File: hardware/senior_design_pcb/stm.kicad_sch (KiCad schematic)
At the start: 44 parts, among them J1 SBH11-PBPC-D05-ST-BK, J2 USB_C_Receptacle_USB2.0_16P, SW1 SW_Push, U1 LD1117S33TR_SOT223, U2 STM32F091RCTx, U3 FT232RL, X1 32.768kHz(12.5pF), X3 8MHz(20pF)

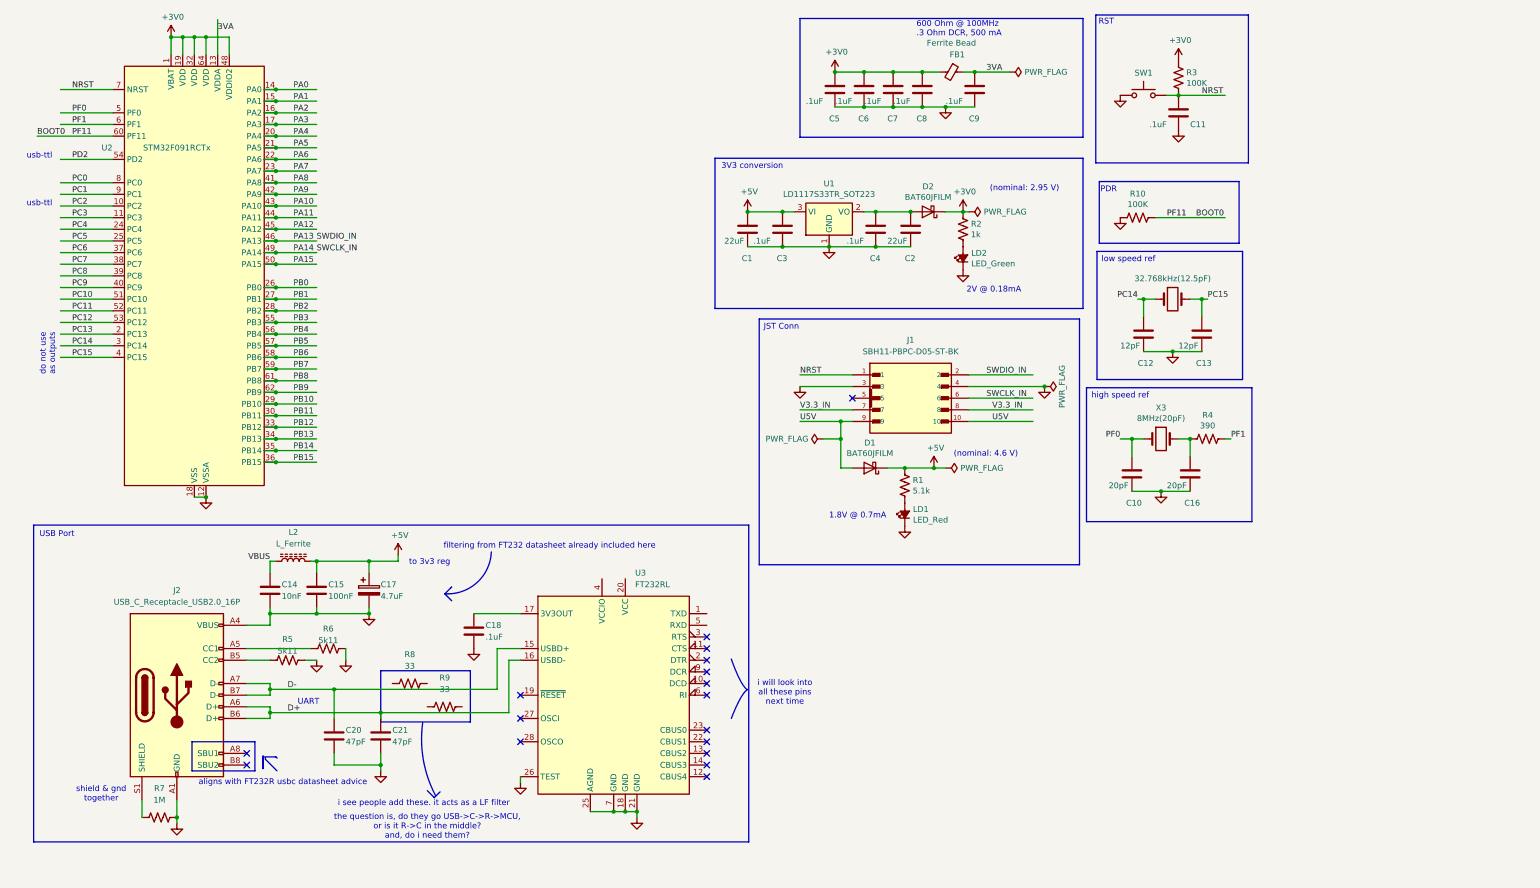
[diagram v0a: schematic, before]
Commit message: made some finishing touches to FT232
removed questionable resistors
confirmed no CBUS
confirmed no external osc
setup bus power
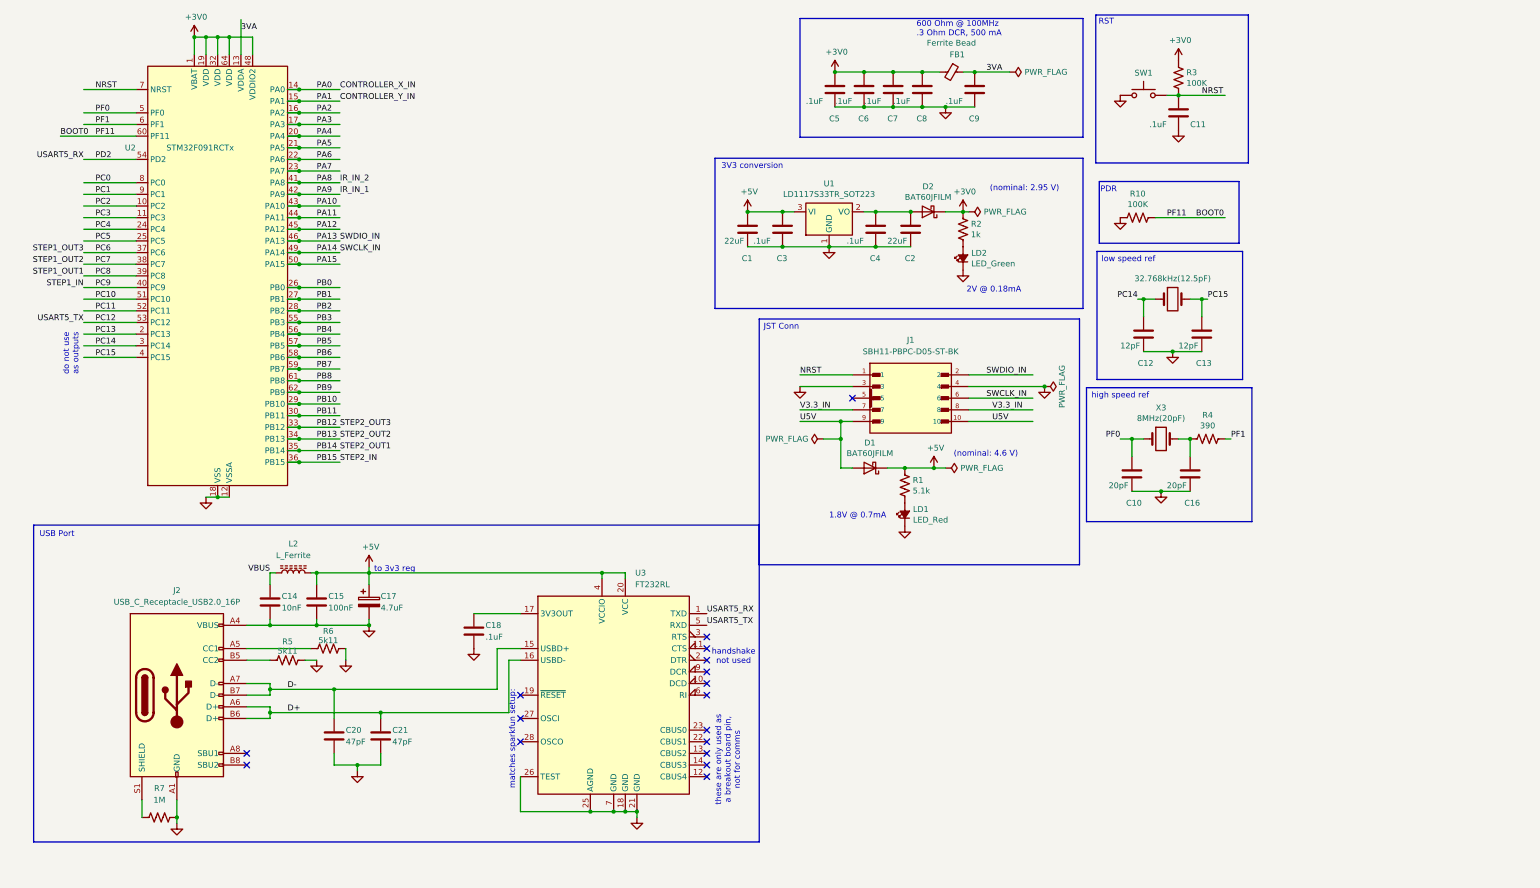
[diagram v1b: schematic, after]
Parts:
- removed R8, R9: 33, symbol Device:R_US
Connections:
- net +5V: now also U3.20 (VCC), U3.4 (VCCIO)
- net PC12: now also U3.5 (RXD)
- net PD2: now also U3.1 (TXD)
- net PA0 renamed CONTROLLER_X_IN
- net PA1 renamed CONTROLLER_Y_IN
- net PA8 renamed IR_IN_2
- net PA9 renamed IR_IN_1
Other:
- note added: "handshake not used"
- note added: "matches sparkfun setup:"
- note added: "these are only used as a breakout board pin, not for comms"
- note removed: "UART"
- note removed: "aligns with FT232R usbc datasheet advice"
- note removed: "filtering from FT232 datasheet already included here"
- note removed: "i see people add these. it acts as a LF filter"
- note removed: "i will look into all these pins next time"
- note removed: "shield & gnd together"
- note removed: "the question is, do they go USB->C->R->MCU, or is it R->C in the middle? and, do i need them?"
- note removed: "usb-ttl"
- moved on the sheet: C14, C15, C17, L2, U2

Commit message: Overall formatting (kicad and CubeIDE)
E96 values
Labels
Pin editing (accidentally used BOOT0)
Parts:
- added J3, J5, J6: Conn_01x03_Socket, symbol Connector:Conn_01x03_Socket
- added J4: Conn_02x08_Odd_Even, Connector_PinSocket_2.54mm:PinSocket_2x08_P2.54mm_Vertical, symbol Connector_Generic:Conn_02x08_Odd_Even
- C10, C16: value 20pF -> 22pf
- R1: value 5.1k -> 5k11
- R4: value 390 -> 392
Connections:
- net GND: now also J4.16 (Pin_16), J4.4 (Pin_4), J4.8 (Pin_8)
- net PB1: now also J4.5 (Pin_5)
- net PB11: now also J4.1 (Pin_1)
- net PA2 renamed OE
- net OE: now also J4.15 (Pin_15)
- net PA3 renamed LAT
- net LAT: now also J4.14 (Pin_14)
- net PA4 renamed CLK
- net CLK: now also J4.13 (Pin_13)
- net PA5 renamed D
- net D: now also J4.12 (Pin_12)
- net PA6 renamed C
- net C: now also J4.11 (Pin_11)
- net PA7 renamed B
- net B: now also J4.10 (Pin_10)
- net PB0 renamed G2
- net G2: now also J4.6 (Pin_6)
- net PB10 renamed G1
- net G1: now also J4.2 (Pin_2)
- net PB2 renamed B1
- net B1: now also J4.3 (Pin_3)
- net PC0 renamed CONTROLLER_X
- net PC1 renamed CONTROLLER_Y
- net PC14 renamed LS_CLK-IN
- net PC15 renamed LS_CLK-OUT
- net PC4 renamed A
- net A: now also J4.9 (Pin_9)
- net PC5 renamed B2
- net B2: now also J4.7 (Pin_7)
- net PF0 renamed HS_CLK-IN
- net PF1 renamed HS_CLK-OUT
- new net ADMIN_JOYSTICK-BUTTON: J5.3 (Pin_3)
- new net ADMIN_JOYSTICK-X: J5.1 (Pin_1)
- new net ADMIN_JOYSTICK-Y: J5.2 (Pin_2)
- new net CONSOLE_DISP-1: J3.1 (Pin_1)
- new net CONSOLE_DISP-2: J3.2 (Pin_2)
- new net CONSOLE_DISP-3: J3.3 (Pin_3)
- new net USER_JOYSTICK-BUTTON: J6.3 (Pin_3)
- new net USER_JOYSTICK-X: J6.1 (Pin_1)
- new net USER_JOYSTICK-Y: J6.2 (Pin_2)
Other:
- note added: "Admin Controller"
- note added: "Admin LCD Console"
- note added: "LED Matrix conn"
- note added: "UI"
- note added: "User Controller"
- note removed: "do not use as outputs"
- note removed: "handshake not used"
- note removed: "matches sparkfun setup:"
- note removed: "these are only used as a breakout board pin, not for comms"
- moved on the sheet: C1, C14, C15, C17, C18, C2, C20, C21, C3, C4, D2, J2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

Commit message: small tweaks
added connectors
added shapes
added button
moved shapes
made bigger sheet
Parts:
- added C19: .1uF, Capacitor_SMD:C_0805_2012Metric_Pad1.15x1.40mm_HandSolder, symbol Device:C
- added J10, J9: Screw_Terminal_01x06, symbol Connector:Screw_Terminal_01x06
- added J7, J8: Conn_01x03_Socket, symbol Connector:Conn_01x03_Socket
- added R8: 100K, Resistor_SMD:R_0805_2012Metric_Pad1.15x1.40mm_HandSolder, symbol Device:R_US
- added SW2: SW_Push, Connector_PinHeader_1.00mm:PinHeader_1x02_P1.00mm_Vertical, symbol Switch:SW_Push
- J3, J5, J6: value Conn_01x03_Socket -> 1x03 Socket
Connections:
- net PA10 is gone; now on net ADMIN_JOYSTICK-BUTTON: U2.43 (PA10)
- net PA11 is gone; now on net ADMIN_JOYSTICK-Y: U2.44 (PA11)
- net PA12 is gone; now on net ADMIN_JOYSTICK-X: U2.45 (PA12)
- net PA15 is gone; now on net CONSOLE_DISP-3: U2.50 (PA15)
- net PC10 is gone; now on net CONSOLE_DISP-2: U2.51 (PC10)
- net PC11 is gone; now on net CONSOLE_DISP-1: U2.52 (PC11)
- net USER_JOYSTICK-BUTTON is gone; now on net PC2: J6.3 (Pin_3)
- net USER_JOYSTICK-X is gone; now on net PC0: J6.1 (Pin_1)
- net USER_JOYSTICK-Y is gone; now on net PC1: J6.2 (Pin_2)
- net +3V0: now also R8.1
- net +5V: now also J7.1 (Pin_1), J8.1 (Pin_1)
- net GND: now also C19.2, J10.6 (Pin_6), J7.3 (Pin_3), J8.3 (Pin_3), J9.6 (Pin_6), SW2.1
- net IR_IN_1: now also J7.2 (Pin_2)
- net IR_IN_2: now also J8.2 (Pin_2)
- net PB12: now also J9.2 (Pin_2)
- net PB13: now also J9.3 (Pin_3)
- net PB14: now also J9.4 (Pin_4)
- net PB15: now also J9.5 (Pin_5)
- net PC6: now also J10.2 (Pin_2)
- net PC7: now also J10.3 (Pin_3)
- net PC8: now also J10.4 (Pin_4)
- net PC9: now also J10.5 (Pin_5)
- net CONTROLLER_X renamed PC0
- net CONTROLLER_Y renamed PC1
- net PB3 renamed ADMIN_CONSOLE-BUTTON
- net ADMIN_CONSOLE-BUTTON: now also C19.1, R8.2, SW2.2
- new net +12V: J10.1 (Pin_1), J9.1 (Pin_1)
- no-connect marks 17 -> 25
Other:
- note added: "Console Button"
- note added: "IR LEDs"
- note added: "STM"
- note added: "Sensor 1"
- note added: "Sensor 2"
- note added: "Stepper Driver"
- moved on the sheet: C1, C10, C11, C12, C13, C14, C15, C16, C17, C18, C2, C20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

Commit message: made it look nice
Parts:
- C14, C15, C17, C18, C20, C21: footprint (none) -> Capacitor_SMD:C_0805_2012Metric_Pad1.15x1.40mm_HandSolder
- L2: footprint (none) -> Resistor_SMD:R_0805_2012Metric_Pad1.15x1.40mm_HandSolder
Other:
- note added: "BOOT0 PDR"
- note added: "MCU Reqs"
- note added: "Periph conn"
- note added: "VDD Filtering"
- note removed: "PDR"
- moved on the sheet: C1, C10, C11, C12, C13, C14, C15, C16, C17, C18, C19, C2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
